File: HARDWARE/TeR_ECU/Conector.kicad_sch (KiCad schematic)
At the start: 15 parts, among them IC1 MX34040NF2, IC2 BTT62004ESAXUMA1

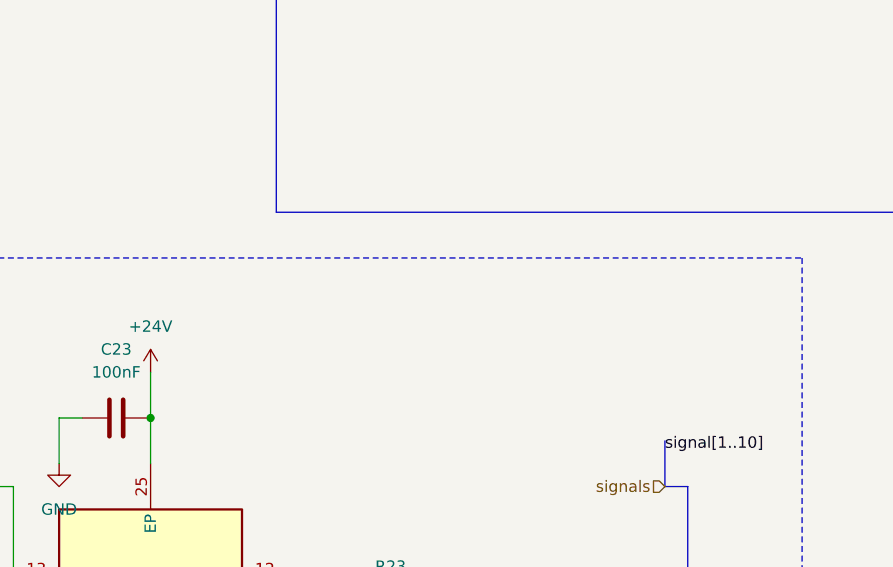
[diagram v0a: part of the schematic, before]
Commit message: sd añadida, uniport redundante eliminado
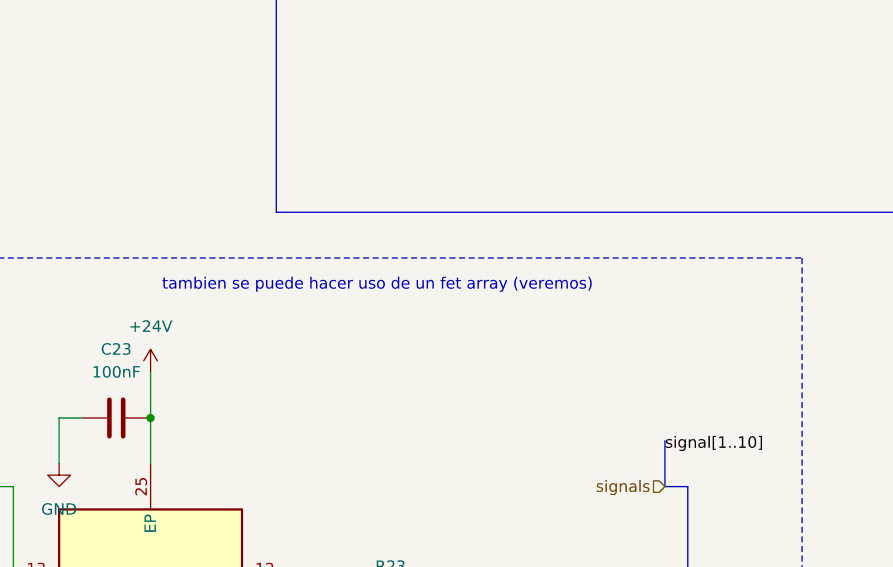
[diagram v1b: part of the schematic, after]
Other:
- note added: "tambien se puede hacer uso de un fet array (veremos)"
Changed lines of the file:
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@@
+    (effects (font (size 1.27 1.27)) (justify left bottom))
+  )
+  (text "tambien se puede hacer uso de un fet array (veremos)"
+    (at 203.2 57.15 0)
     (effects (font (size 1.27 1.27)) (justify left bottom))
   )

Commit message: Quick changes
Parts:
- removed C23: 100nF, symbol Device:C
- removed C24, C25, C26, C27: 10nF, symbol Device:C
- removed IC2: BTT62004ESAXUMA1, SOP65P600X115-25N, symbol BTT62004ESAXUMA1:BTT62004ESAXUMA1
- removed R22, R23, R24, R25: 10K, symbol Device:R
- removed R26, R27, R28, R29: 47K, symbol Device:R
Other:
- note removed: "NOTAS"
- note removed: "esta es la idea, conseguir shiftear la señal 3.3 a 24v de momento usaremos este ic, pero lo que realmente importa es la idea"
- note removed: "tambien se puede hacer uso de un fet array (veremos)"
- moved on the sheet: IC1

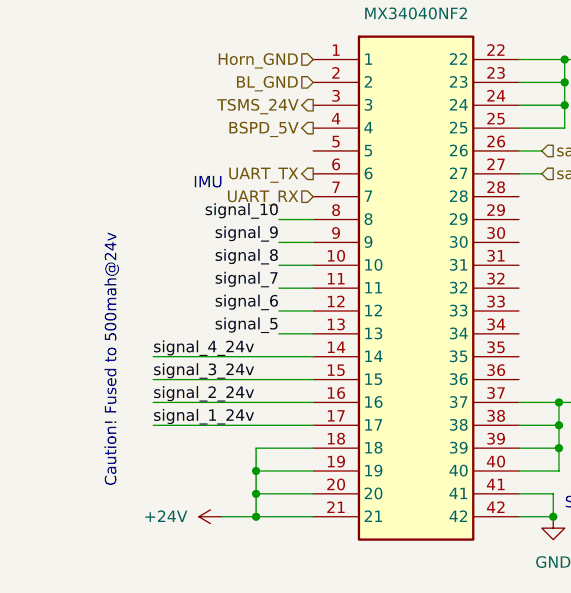
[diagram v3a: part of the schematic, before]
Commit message: Advanced design and added IMU/GPS moduleç
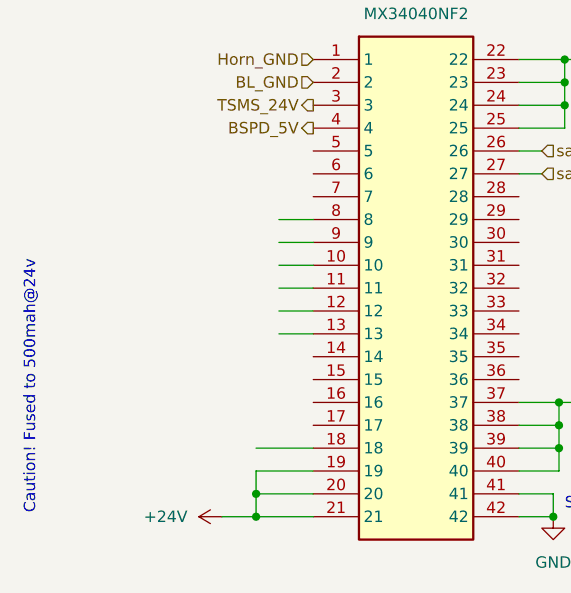
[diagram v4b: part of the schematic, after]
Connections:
- net +24V: no longer IC1.18
- net UART_RX: no longer names the net of IC1.7
- net UART_TX: no longer names the net of IC1.6
- net signal_10: no longer names the net of IC1.8
- net signal_1_24v: no longer names the net of IC1.17
- net signal_2_24v: no longer names the net of IC1.16
- net signal_3_24v: no longer names the net of IC1.15
- net signal_4_24v: no longer names the net of IC1.14
- net signal_5: no longer names the net of IC1.13
- net signal_6: no longer names the net of IC1.12
- net signal_7: no longer names the net of IC1.11
- net signal_8: no longer names the net of IC1.10
- net signal_9: no longer names the net of IC1.9
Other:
- note removed: "IMU"
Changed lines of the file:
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@@
-	)
-	(junction
-		(at 124.46 115.57)
-		(diameter 0)
-		(color 0 0 0 0)
 	)
 	(junction
@@
 	(wire
 		(pts
-			(xy 113.03 110.49) (xy 130.81 110.49)
-		)
-		(stroke
-			(width 0)
-			(type default)
-		)
-	)
-	(wire
-		(pts
 			(xy 127 97.79) (xy 130.81 97.79)
 		)
@@
 	(wire
 		(pts
-			(xy 113.03 107.95) (xy 130.81 107.95)
-		)
-		(stroke
-			(width 0)
-			(type default)
-		)
-	)
-	(wire
-		(pts
 			(xy 158.115 115.57) (xy 158.115 113.03)
 		)
@@
 	(wire
 		(pts
-			(xy 124.46 115.57) (xy 124.46 113.03)
-		)
-		(stroke
-			(width 0)
-			(type default)
-		)
-	)
-	(wire
-		(pts
 			(xy 158.115 110.49) (xy 153.67 110.49)
 		)
@@
 	(wire
 		(pts
-			(xy 113.03 102.87) (xy 130.81 102.87)
-		)
-		(stroke
-			(width 0)
-			(type default)
-		)
-	)
-	(wire
-		(pts
 			(xy 124.46 120.65) (xy 124.46 118.11)
 		)
@@
 	(wire
 		(pts
-			(xy 113.03 105.41) (xy 130.81 105.41)
-		)
-		(stroke
-			(width 0)
-			(type default)
-		)
-	)
-	(wire
-		(pts
 			(xy 120.65 120.65) (xy 124.46 120.65)
 		)
@@
 			(width 0)
 			(type default)
-		)
-	)
-	(text "IMU"
-		(exclude_from_sim no)
-		(at 117.475 84.455 0)
-		(effects
-			(font
-				(size 1.27 1.27)
-			)
-			(justify left bottom)
 		)
 	)
 	(text "Caution! Fused to 500mah@24v\n\n"
 		(exclude_from_sim no)
-		(at 111.125 117.475 90)
+		(at 102.108 120.396 90)
 		(effects
 			(font
@@
 		)
 	)
-	(label "signal_1_24v"
-		(at 113.03 110.49 0)
-		(fields_autoplaced yes)
-		(effects
-			(font
-				(size 1.27 1.27)
-			)
-			(justify left bottom)
-		)
-	)
-	(label "signal_10"
-		(at 127 87.63 180)
-		(fields_autoplaced yes)
-		(effects
-			(font
-				(size 1.27 1.27)
-			)
-			(justify right bottom)
-		)
-	)
-	(label "signal_2_24v"
-		(at 113.03 107.95 0)
-		(fields_autoplaced yes)
-		(effects
-			(font
-				(size 1.27 1.27)
-			)
-			(justify left bottom)
-		)
-	)
-	(label "signal_6"
-		(at 127 97.79 180)
-		(fields_autoplaced yes)
-		(effects
-			(font
-				(size 1.27 1.27)
-			)
-			(justify right bottom)
-		)
-	)
-	(label "signal_5"
-		(at 127 100.33 180)
-		(fields_autoplaced yes)
-		(effects
-			(font
-				(size 1.27 1.27)
-			)
-			(justify right bottom)
-		)
-	)
-	(label "signal_9"
-		(at 127 90.17 180)
-		(fields_autoplaced yes)
-		(effects
-			(font
-				(size 1.27 1.27)
-			)
-			(justify right bottom)
-		)
-	)
-	(label "signal_8"
-		(at 127 92.71 180)
-		(fields_autoplaced yes)
-		(effects
-			(font
-				(size 1.27 1.27)
-			)
-			(justify right bottom)
-		)
-	)
-	(label "signal_4_24v"
-		(at 113.03 102.87 0)
-		(fields_autoplaced yes)
-		(effects
-			(font
-				(size 1.27 1.27)
-			)
-			(justify left bottom)
-		)
-	)
-	(label "signal_7"
-		(at 127 95.25 180)
-		(fields_autoplaced yes)
-		(effects
-			(font
-				(size 1.27 1.27)
-			)
-			(justify right bottom)
-		)
-	)
-	(label "signal_3_24v"
-		(at 113.03 105.41 0)
-		(fields_autoplaced yes)
-		(effects
-			(font
-				(size 1.27 1.27)
-			)
-			(justify left bottom)
-		)
-	)
 	(hierarchical_label "BSPD_5V"
 		(shape output)
@@
 		(shape output)
 		(at 130.81 74.93 180)
-		(fields_autoplaced yes)
-		(effects
-			(font
-				(size 1.27 1.27)
-			)
-			(justify right)
-		)
-	)
-	(hierarchical_label "UART_RX"
-		(shape input)
-		(at 130.81 85.09 180)
-		(fields_autoplaced yes)
-		(effects
-			(font
-				(size 1.27 1.27)
-			)
-			(justify right)
-		)
-	)
-	(hierarchical_label "UART_TX"
-		(shape output)
-		(at 130.81 82.55 180)
 		(fields_autoplaced yes)
 		(effects
@@
 		(dnp no)
 		(fields_autoplaced yes)
-		(property "Reference" "#PWR09"
+		(property "Reference" "#PWR045"
 			(at 167.64 69.85 0)
 			(effects
@@
 			(project "TeR_ECU"
 				(path "/84413845-c4f3-4743-bcd2-a67649c90902/e25d0f8a-65a3-47e2-987f-518da8891580"
-					(reference "#PWR09")
+					(reference "#PWR045")
 					(unit 1)
 				)
@@
 		(on_board yes)
 		(dnp no)
-		(property "Reference" "#PWR010"
+		(property "Reference" "#PWR046"
 			(at 124.46 120.65 0)
 			(effects
@@
 			(project "TeR_ECU"
 				(path "/84413845-c4f3-4743-bcd2-a67649c90902/e25d0f8a-65a3-47e2-987f-518da8891580"
-					(reference "#PWR010")
+					(reference "#PWR046")
 					(unit 1)
 				)
@@
 		(dnp no)
 		(fields_autoplaced yes)
-		(property "Reference" "#PWR02"
+		(property "Reference" "#PWR047"
 			(at 157.48 127 0)
 			(effects
@@
 			(project "TeR_ECU"
 				(path "/84413845-c4f3-4743-bcd2-a67649c90902/e25d0f8a-65a3-47e2-987f-518da8891580"
-					(reference "#PWR02")
+					(reference "#PWR047")
 					(unit 1)
 				)

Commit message: Quick changes, go to start layouting
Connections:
- net GND: no longer IC1.22, IC1.23, IC1.24, IC1.25, IC1.41
- removed net +24V: IC1.19, IC1.20, IC1.21
- removed net 24v_NF: IC1.37, IC1.38, IC1.39, IC1.40
- net BL_GND: no longer names the net of IC1.2
- net BSPD_5V: no longer names the net of IC1.4
- net Horn_GND: no longer names the net of IC1.1
- net TSMS_24V: no longer names the net of IC1.3
- net safety_in: no longer names the net of IC1.26
- net safety_out: no longer names the net of IC1.27
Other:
- note removed: "Non Fused Outputs"
- note removed: "Sujecciones"
